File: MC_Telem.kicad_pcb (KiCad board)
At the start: 2 copper layers, 100 x 100 mm, 59 parts, among them J1 Conn_ARM_JTAG_SWD_10, J2 USB_B_Micro, J3 34830-0801, J5 Conn_01x05, J7 DB37_Male_MountingHoles, J8 34830-0801, J9 GPS, Q1 Q_NMOS_GDS, Q2 Q_NMOS_GDS, Q20 AO4407A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

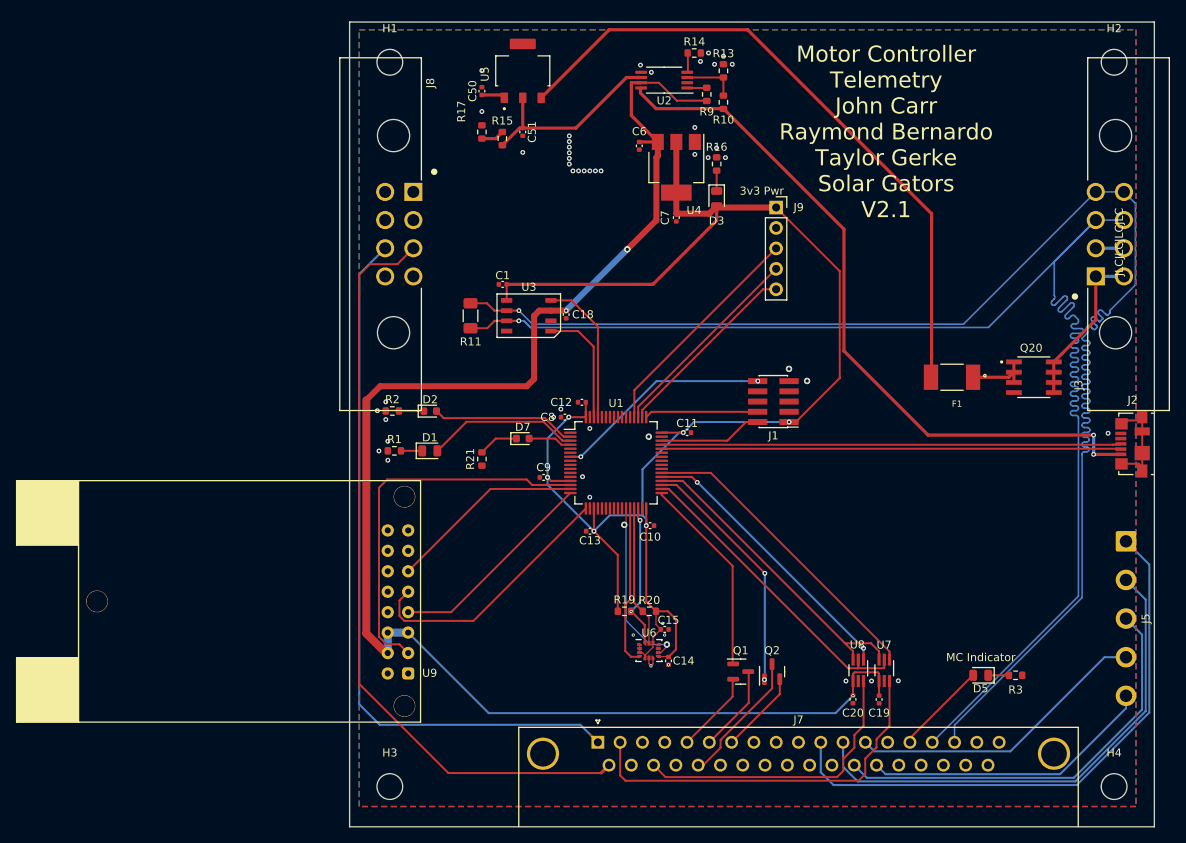
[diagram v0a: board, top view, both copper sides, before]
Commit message: FSGP MC Telemetry Hardware
Final PCB revision used for Sunrider at FSGP 2023
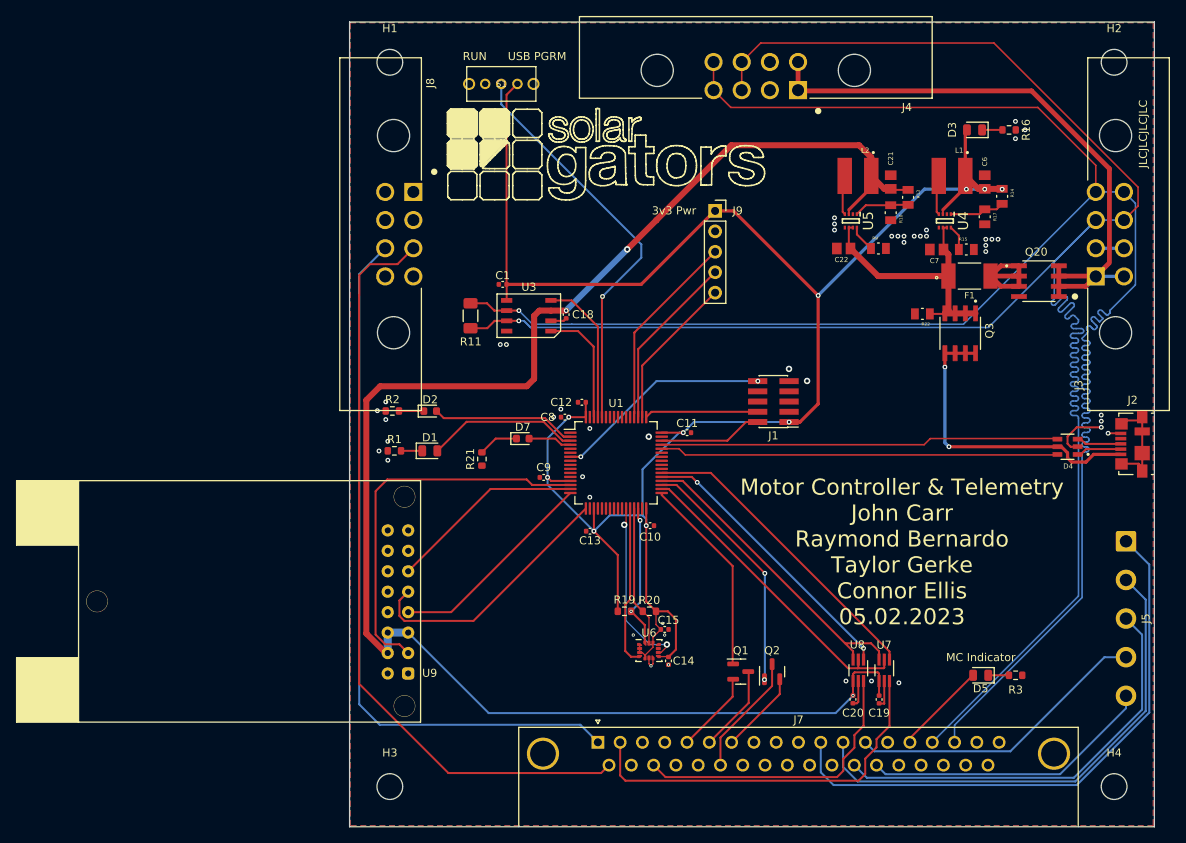
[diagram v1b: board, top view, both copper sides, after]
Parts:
- removed C50, C51: 10uF, Capacitor_SMD:C_0402_1005Metric
- removed U2: TPS2113, Package_SO:TSSOP-8_4.4x3mm_P0.65mm
- added C21: CL21A226MAQNNNE, CL21A226MAQNNNE:CAPC2012X140N, F.Cu at (142.2, 79.9)
- added C22: CL21A226MAQNNNE, CL21A226MAQNNNE:CAPC2012X140N, F.Cu at (136.4, 88.1)
- added D4: USBLC6-2SC6, USBLC6-2SC6:SOT95P280X145-6N, F.Cu at (164.2, 112.8)
- added J4: 34830-0801, 34830-0801 (1):MOLEX_34830-0801, F.Cu at (125.5, 66.0)
- added L1: LVS505040-2R2M-N, SDR0403-2R2ML:IND_SDR0403-2R2ML, F.Cu at (149.9, 79.1)
- added L2: LVS505040-2R2M-N, SDR0403-2R2ML:IND_SDR0403-2R2ML, F.Cu at (138.2, 79.1)
- added Q3: AO4407A, AO4407A (1):SOIC127P600X175-8N, F.Cu at (150.9, 98.7)
- added R22: 0805W8F1803T5E, CR0805AJ_-000EAS:RESC2012X60N, F.Cu at (146.2, 96.3)
- added S1: 1825232-1, 1825232-1:1825232-1, F.Cu at (93.9, 67.7)
- C6, C7: value 1uF -> CL21A226MAQNNNE; footprint Capacitor_SMD:C_0402_1005Metric -> CL21A226MAQNNNE:CAPC2012X140N
- F1: value SMD1812P300TF -> SMD1812P075TF/24
- R10: value 10k -> CR0805F83402G; footprint Resistor_SMD:R_0603_1608Metric -> CR0805AJ_-000EAS:RESC2012X60N
- R13: value 10k -> HPCR0805F249KK9; footprint Resistor_SMD:R_0603_1608Metric -> CR0805AJ_-000EAS:RESC2012X60N
- R14: value 220 -> WR08X2493FTL; footprint Resistor_SMD:R_0603_1608Metric -> CR0805AJ_-000EAS:RESC2012X60N
- R15: value 5.1k -> WR08X9311FTL; footprint Resistor_SMD:R_0603_1608Metric -> CR0805AJ_-000EAS:RESC2012X60N
- R17: value 15k -> CR0805F83402G; footprint Resistor_SMD:R_0603_1608Metric -> CR0805AJ_-000EAS:RESC2012X60N
- R9: value 10k -> WR08X9311FTL; footprint Resistor_SMD:R_0603_1608Metric -> CR0805AJ_-000EAS:RESC2012X60N
- U4: value AMS1117-5.0 -> TPS629206QDRLRQ1; footprint Package_TO_SOT_SMD:SOT-223-3_TabPin2 -> SamacSys_Parts:SOTFL50P160X60-8N
- U5: value AMS1117 -> TPS629206QDRLRQ1; footprint AMS1117 (1):SOT229P700X180-4N -> SamacSys_Parts:SOTFL50P160X60-8N
- moved R17 63.4 mm to (153.9, 84.2)
- moved R15 59.3 mm to (151.6, 88.3), turned to 0 degrees
- moved U5 44.8 mm to (137.3, 84.7), turned to -90 degrees
- moved C6 43.2 mm to (153.9, 79.9), turned to 90 degrees
- moved R14 42.2 mm to (156.1, 81.7), turned to -90 degrees
- moved R16 36.6 mm to (156.9, 73.4), turned to 0 degrees
- moved U4 34.0 mm to (149.0, 84.7)
- moved D3 33.2 mm to (152.7, 73.4), turned to 180 degrees
- moved C7 32.6 mm to (148.0, 88.3), turned to 180 degrees
- moved R9 28.7 mm to (140.7, 88.1), turned to 0 degrees
- moved R13 27.8 mm to (144.4, 81.8), turned to -90 degrees
- moved R10 24.9 mm to (142.2, 83.7), turned to -90 degrees
- moved F1 12.8 mm to (152.0, 91.6), turned to 0 degrees
- moved Q20 12.0 mm to (160.6, 92.2)
- moved J9 7.59 mm to (120.4, 83.5)
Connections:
- C6 pad 1: +5V -> +3V3
- C7 pad 1: +3V3 -> /12V_safe
- F1 pad 1: Net-(F1-Pad1) -> /12V_safe
- F1 pad 2: /12V_safe -> Net-(F1-Pad2)
- J2 pad 2: /D- -> /D-_USB
- J2 pad 3: /D+ -> /D+_USB
- J7 pad 24: /Rev- -> unconnected-(J7-Pad24)
- J7 pad 25: unconnected-(J7-Pad25) -> /Rev-
- Q20 pad 1: Net-(F1-Pad1) -> Net-(F1-Pad2)
- Q20 pad 2: Net-(F1-Pad1) -> Net-(F1-Pad2)
- Q20 pad 3: Net-(F1-Pad1) -> Net-(F1-Pad2)
- R10 pad 1: /5v_USB -> Net-(R10-Pad1)
- R10 pad 2: /VSNS -> GND
- R13 pad 1: /VSNS -> +5V
- R13 pad 2: GND -> Net-(R10-Pad1)
- R14 pad 1: Net-(R14-Pad1) -> +3V3
- R14 pad 2: GND -> Net-(R14-Pad2)
- R15 pad 1: Net-(C50-Pad1) -> Net-(R15-Pad1)
- R15 pad 2: /5v_Reg -> GND
- R17 pad 1: GND -> Net-(R14-Pad2)
- R17 pad 2: Net-(C50-Pad1) -> GND
- R9 pad 1: /PWR_STAT -> Net-(R9-Pad1)
- R9 pad 2: +5V -> GND
- U1 pad 60: unconnected-(U1-Pad60) -> /BOOT
- U4 pad 1: GND -> Net-(R14-Pad2)
- U4 pad 2: +3V3 -> unconnected-(U4-Pad2)
- U4 pad 3: +5V -> +3V3
- U5 pad 1: Net-(C50-Pad1) -> Net-(R10-Pad1)
- U5 pad 2: /5v_Reg -> unconnected-(U5-Pad2)
- U5 pad 3: /12V_safe -> +5V
- U5 pad 4: (no net) -> Net-(L2-Pad2)
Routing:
- net /CAN+: track 188.0 -> 254.0 mm
- net /CAN-: track 188.5 -> 246.7 mm
- net +12V: track 20.1 -> 77.3 mm
- net /BOOT: track 0.00 -> 50.6 mm, vias 0 -> 1
- net /5v_USB: track 89.2 -> 38.5 mm
- net +3V3: track 194.3 -> 243.9 mm, vias 6 -> 10
- net /12V_safe: track 81.9 -> 34.1 mm
- net /5v_Reg: track 24.4 -> 0.00 mm
- net GND: track 5.68 -> 23.1 mm, vias 50 -> 47
- net Net-(F1-Pad2): track 0.00 -> 14.2 mm
- net +5V: track 187.6 -> 201.2 mm
- net Net-(F1-Pad1): track 7.87 -> 0.00 mm
- net /D-: track 57.0 -> 49.5 mm
- net /D+: track 56.9 -> 49.5 mm
- net Net-(R14-Pad2): track 0.00 -> 6.89 mm
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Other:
- board text added: "Motor Controller & Telemetry John Carr Raymond Bernardo Taylor Gerke Connor Ellis 05.02.2023"
- board text added: "RUN"
- board text added: "USB PGRM"
- board text removed: "Motor Controller Telemetry John Carr Raymond Bernardo Taylor Gerke Solar Gators V2.1"
